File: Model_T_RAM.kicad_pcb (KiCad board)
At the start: 2 copper layers, 19.8 x 34.3 mm, 4 parts, among them J1 KC-85_RAM, U1 6264, U2 74HC08

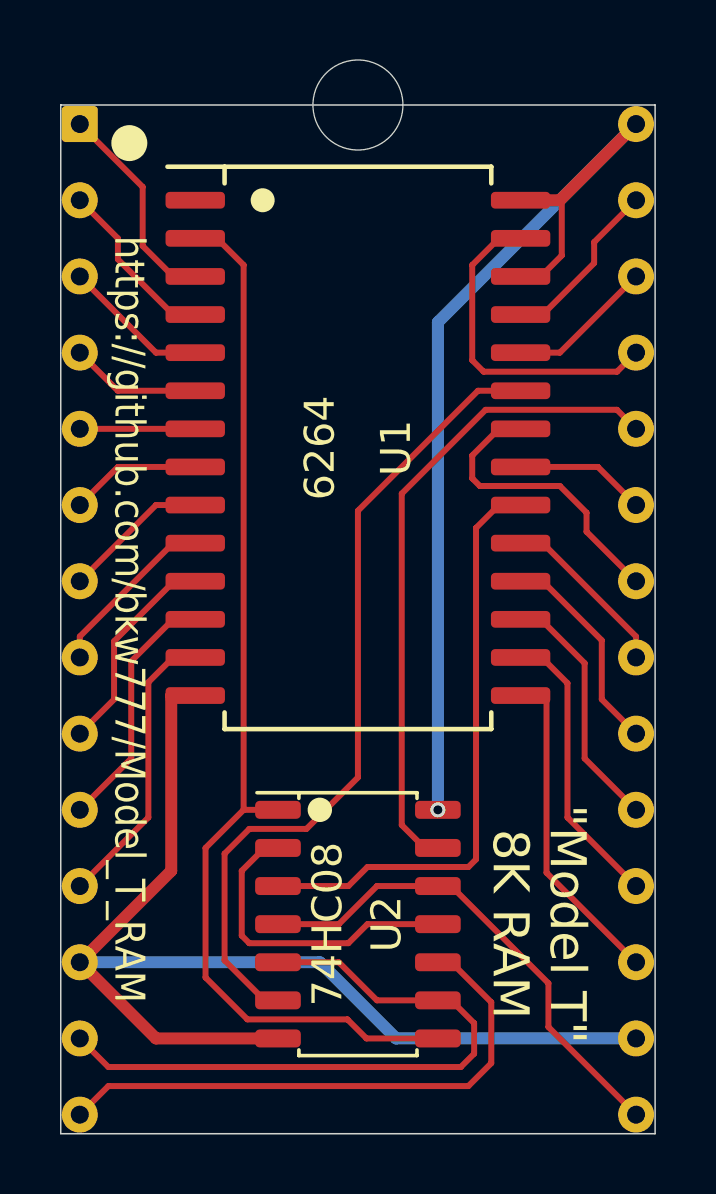
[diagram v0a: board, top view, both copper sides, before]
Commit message: remove 74HC86 b version
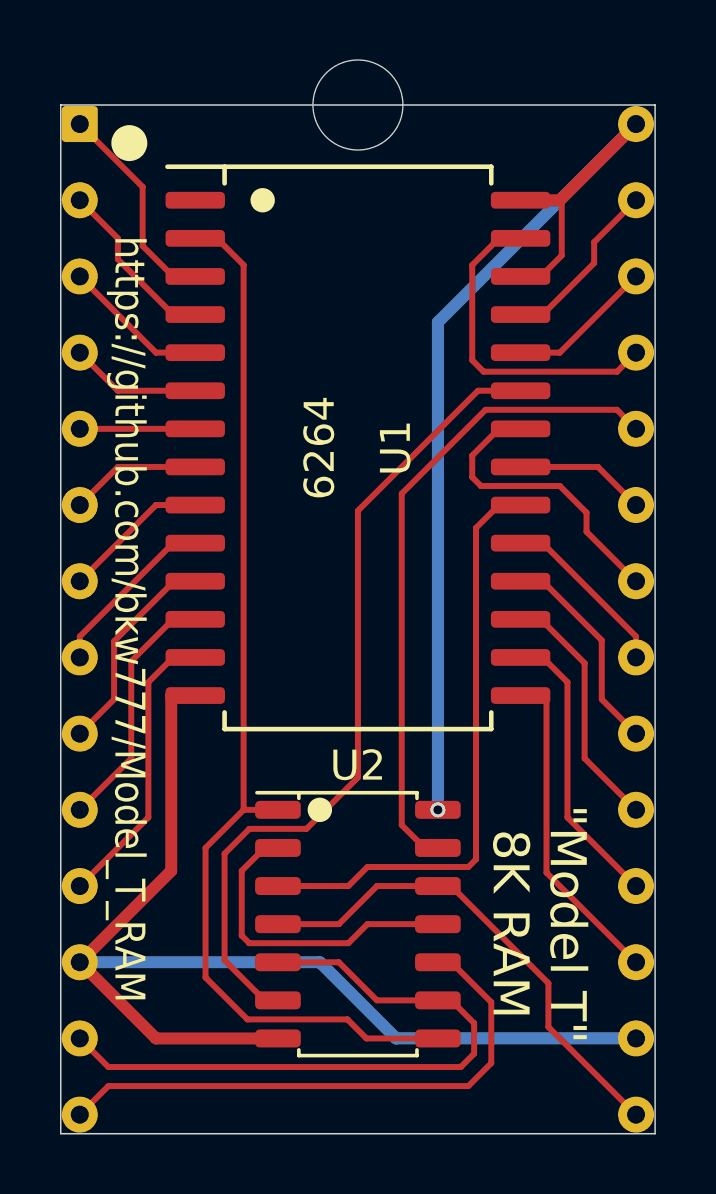
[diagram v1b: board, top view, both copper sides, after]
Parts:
- U2: footprint 000_LOCAL:SOIC-14_3.9x8.7mm_P1.27mm -> 000_LOCAL:SOIC-14_4x9
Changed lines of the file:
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@@
     (add_net /~WE)
     (add_net GND)
+    (add_net "Net-(U1-Pad1)")
     (add_net "Net-(U2-Pad11)")
     (add_net VCC)
   )
-  (module 000_LOCAL:SOIC-14_3.9x8.7mm_P1.27mm (layer F.Cu)
+  (module 000_LOCAL:SOIC-14_4x9 (layer F.Cu)
     (at 142.24 109.22)
     (descr "SOIC, 14 Pin (JEDEC MS-012AB, https://www.analog.com/media/en/package-pcb-resources/package/pkg_pdf/soic_narrow-r/r_14.pdf), generated with kicad-footprint-generator ipc_gullwing_generator.py")
     (tags "SOIC SO")
     (attr smd)
-    (fp_text reference U2 (at 0.9525 0 -90) (layer F.SilkS)
-      (effects (font (size 1 1) (thickness 0.15)))
-    )
-    (fp_text value 74HC08 (at -1.016 0 -90) (layer F.SilkS)
-      (effects (font (size 1 1) (thickness 0.15)))
+    (fp_text reference U2 (at 0 -5.28) (layer F.SilkS)
+      (effects (font (size 1 1) (thickness 0.15)))
+    )
+    (fp_text value 74HC08 (at 0 5.28) (layer F.Fab)
+      (effects (font (size 1 1) (thickness 0.15)))
+    )
+    (fp_text user %R (at 0 0) (layer F.Fab)
+      (effects (font (size 0.98 0.98) (thickness 0.15)))
     )
     (fp_circle (center -1.27 -3.81) (end -1.0668 -3.81) (layer F.SilkS) (width 0.4064))
@@
     (fp_line (start 3.7 4.58) (end 3.7 -4.58) (layer F.CrtYd) (width 0.05))
     (fp_line (start 3.7 -4.58) (end -3.7 -4.58) (layer F.CrtYd) (width 0.05))
-    (fp_text user %R (at 0 0) (layer F.Fab)
-      (effects (font (size 0.98 0.98) (thickness 0.15)))
-    )
     (pad 14 smd roundrect (at 2.6655 -3.81) (size 1.524 0.6) (layers F.Cu F.Paste F.Mask) (roundrect_rratio 0.25)
       (net 6 VCC))
@@
       (effects (font (size 1 1) (thickness 0.15)))
     )
-    (fp_circle (center -3.175 -8.255) (end -2.975 -8.255) (layer F.SilkS) (width 0.4))
+    (fp_line (start -4.445 9.3726) (end 4.445 9.3726) (layer F.SilkS) (width 0.1524))
+    (fp_line (start 4.445 9.3726) (end 4.445 8.81634) (layer F.SilkS) (width 0.1524))
+    (fp_line (start 4.445 -9.3726) (end -6.35 -9.3726) (layer F.SilkS) (width 0.1524))
+    (fp_line (start -4.445 -9.3726) (end -4.445 -8.81634) (layer F.SilkS) (width 0.1524))
+    (fp_line (start -4.445 8.81634) (end -4.445 9.3726) (layer F.SilkS) (width 0.1524))
     (fp_line (start 4.445 -8.81634) (end 4.445 -9.3726) (layer F.SilkS) (width 0.1524))
-    (fp_line (start -4.445 8.81634) (end -4.445 9.3726) (layer F.SilkS) (width 0.1524))
-    (fp_line (start -4.445 -9.3726) (end -4.445 -8.81634) (layer F.SilkS) (width 0.1524))
-    (fp_line (start 4.445 -9.3726) (end -6.35 -9.3726) (layer F.SilkS) (width 0.1524))
-    (fp_line (start 4.445 9.3726) (end 4.445 8.81634) (layer F.SilkS) (width 0.1524))
-    (fp_line (start -4.445 9.3726) (end 4.445 9.3726) (layer F.SilkS) (width 0.1524))
+    (fp_circle (center -3.175 -8.255) (end -2.9718 -8.255) (layer F.SilkS) (width 0.4064))
     (pad 28 smd roundrect (at 5.4229 -8.255) (size 1.9812 0.5588) (layers F.Cu F.Paste F.Mask) (roundrect_rratio 0.25)
       (net 6 VCC))
@@
       (effects (font (size 1 1) (thickness 0.15)))
     )
+    (fp_line (start -9.8806 -17.1196) (end -9.8806 17.1196) (layer F.CrtYd) (width 0.01))
+    (fp_line (start -9.8806 17.1196) (end 9.8806 17.1196) (layer F.CrtYd) (width 0.01))
+    (fp_line (start 9.8806 17.1196) (end 9.8806 -17.1196) (layer F.CrtYd) (width 0.01))
     (fp_line (start 9.8806 -17.1196) (end -9.8806 -17.1196) (layer F.CrtYd) (width 0.01))
-    (fp_line (start 9.8806 17.1196) (end 9.8806 -17.1196) (layer F.CrtYd) (width 0.01))
-    (fp_line (start -9.8806 17.1196) (end 9.8806 17.1196) (layer F.CrtYd) (width 0.01))
-    (fp_line (start -9.8806 -17.1196) (end -9.8806 17.1196) (layer F.CrtYd) (width 0.01))
     (fp_text user %R (at 0 0 -90) (layer F.Fab)
       (effects (font (size 1 1) (thickness 0.15)))
@@
   (segment (start 134.239 91.44) (end 132.969 90.17) (width 0.2) (layer F.Cu) (net 13))
   (segment (start 136.8171 91.44) (end 134.239 91.44) (width 0.2) (layer F.Cu) (net 13))
-  (segment (start 148.36775 100.33) (end 147.6629 100.33) (width 0.2) (layer F.Cu) (net 14))
-  (segment (start 149.225 101.18725) (end 148.36775 100.33) (width 0.2) (layer F.Cu) (net 14))
-  (segment (start 149.225 105.664) (end 149.225 101.18725) (width 0.2) (layer F.Cu) (net 14))
+  (segment (start 148.3995 100.33) (end 147.6629 100.33) (width 0.2) (layer F.Cu) (net 14))
+  (segment (start 149.225 101.1555) (end 148.3995 100.33) (width 0.2) (layer F.Cu) (net 14))
+  (segment (start 149.225 105.664) (end 149.225 101.1555) (width 0.2) (layer F.Cu) (net 14))
   (segment (start 151.511 107.95) (end 149.225 105.664) (width 0.2) (layer F.Cu) (net 14))
   (segment (start 132.969 92.71) (end 136.8171 92.71) (width 0.2) (layer F.Cu) (net 15))
@@
   (segment (start 146.939 92.71) (end 147.6629 92.71) (width 0.2) (layer F.Cu) (net 22))
   (segment (start 146.05 93.599) (end 146.939 92.71) (width 0.2) (layer F.Cu) (net 22))
-  (segment (start 146.05 94.361) (end 146.05 93.599) (width 0.2) (layer F.Cu) (net 22))
-  (segment (start 146.304 94.615) (end 146.05 94.361) (width 0.2) (layer F.Cu) (net 22))
-  (segment (start 148.971 94.615) (end 146.304 94.615) (width 0.2) (layer F.Cu) (net 22))
+  (segment (start 146.05 94.3229) (end 146.05 93.599) (width 0.2) (layer F.Cu) (net 22))
+  (segment (start 146.3421 94.615) (end 146.05 94.3229) (width 0.2) (layer F.Cu) (net 22))
+  (segment (start 148.971 94.615) (end 146.3421 94.615) (width 0.2) (layer F.Cu) (net 22))
   (segment (start 149.86 95.504) (end 148.971 94.615) (width 0.2) (layer F.Cu) (net 22))
   (segment (start 149.86 96.139) (end 149.86 95.504) (width 0.2) (layer F.Cu) (net 22))
